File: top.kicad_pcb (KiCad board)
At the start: 2 copper layers, 49.5 x 147.2 mm, 61 parts, among them J1 Conn_01x04, J10 105162-0001, J2 USB_B_Micro, J3 Conn_01x02, J4 Conn_01x02, J5 Conn_01x02, J6 Conn_01x04, J7 Conn_01x02, J8 Conn_01x02, J9 Conn_01x02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

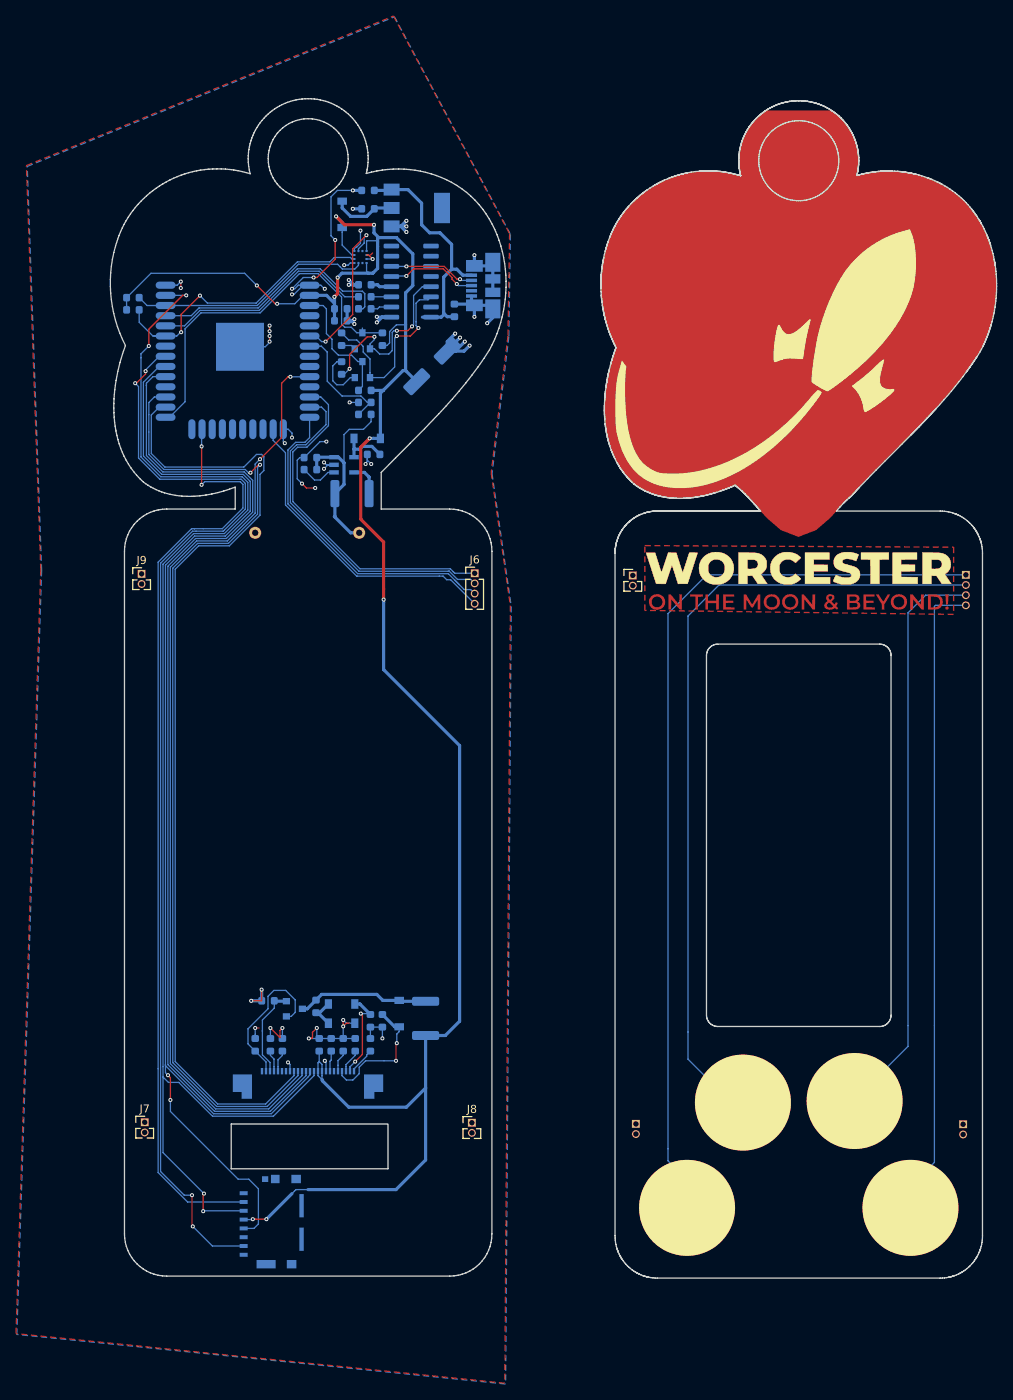
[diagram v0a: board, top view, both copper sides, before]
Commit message: split boards into top and bottom
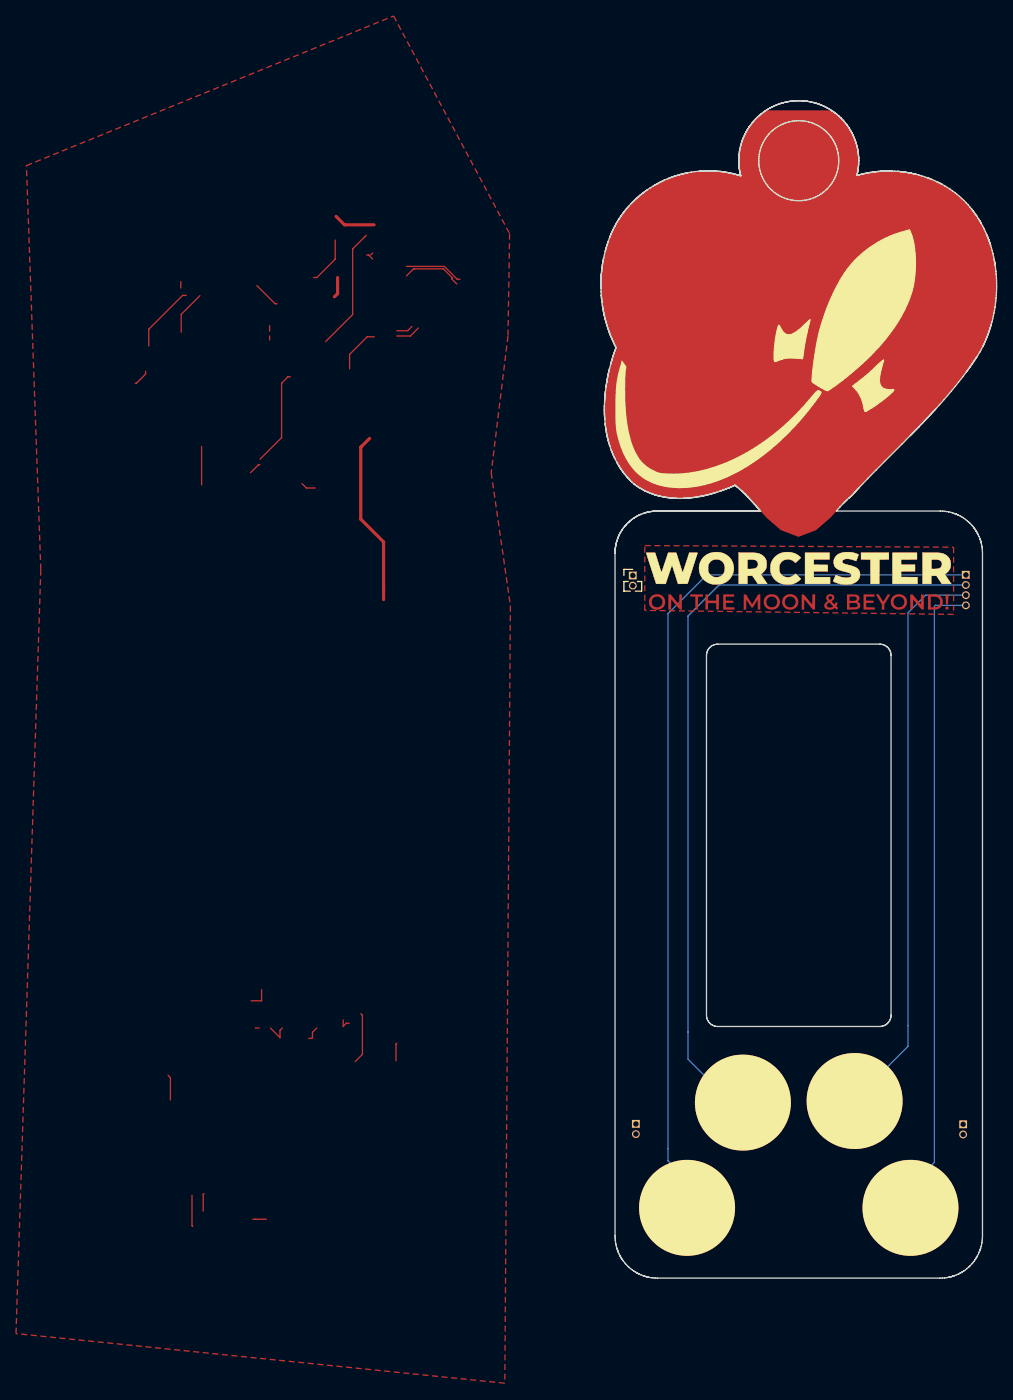
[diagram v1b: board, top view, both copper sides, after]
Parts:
- removed BT1: Battery_Cell, 12BH321P-GR:12BH321P-GR
- removed C1, C17, C2, C3: 10uF, Capacitor_SMD:C_0603_1608Metric
- removed C10, C11, C12, C13, C16, C18, C20, C4, C6, C7, C8, C9: 1uF, Capacitor_SMD:C_0603_1608Metric
- removed C14: 2.2uF, Capacitor_SMD:C_0603_1608Metric
- removed C19: 220uF, Capacitor_SMD:CP_Elec_6.3x5.7
- removed C5: 10uf, Capacitor_SMD:C_0603_1608Metric
- removed D1, D2, D3, D4, D5: D_Schottky, Diode_SMD:D_SOD-123
- removed J10: 105162-0001, 105162-0001:105162-0001
- removed J2: USB_B_Micro, Connector_USB:USB_Micro-B_Molex_47346-0001
- removed J6: Conn_01x04, Connector_PinHeader_1.27mm:PinHeader_1x04_P1.27mm_Vertical
- removed J7, J8, J9: Conn_01x02, Connector_PinHeader_1.27mm:PinHeader_1x02_P1.27mm_Vertical
- removed L1: L, Inductor_SMD:L_1812_4532Metric
- removed L2: 68uH, Inductor_SMD:L_1812_4532Metric
- removed Q1, Q3: PN2222A, Package_TO_SOT_SMD:SOT-23
- removed Q2: Q_NMOS_GSD, Package_TO_SOT_SMD:SOT-23
- removed R1: 10KR, Capacitor_SMD:C_0603_1608Metric
- removed R10, R3, R5, R6: 10K, Capacitor_SMD:C_0603_1608Metric
- removed R11, R8: 1k, Capacitor_SMD:C_0603_1608Metric
- removed R12, R13: 2.2k, Capacitor_SMD:C_0603_1608Metric
- removed R2: DNP, Capacitor_SMD:C_0603_1608Metric
- removed R4: 2.2R, Capacitor_SMD:C_0603_1608Metric
- removed R7, R9: 100k, Capacitor_SMD:C_0603_1608Metric
- removed U1: ESP32-WROOM, ESP32-footprints-Lib:ESP32-WROOM
- removed U2: XC9141, SOT95P280X130-5N:SOT95P280X130-5N
- removed U3: KX122-1037, LGA16R50P4X4_200X200X100:LGA16R50P4X4_200X200X100
- removed U4: AP1117-33, Package_TO_SOT_SMD:SOT-223-3_TabPin2
- removed U5: CH340G, Package_SO:SOIC-16_3.9x9.9mm_P1.27mm
- removed X1: 52435-2471, 52435-2471:MOLEX_52435-2471
- removed the svg2mod at (140.0, 100.0)
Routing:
- net +3V3: track 249.6 -> 34.7 mm, vias 10 -> 0
- net EINK_MOSI: track 168.6 -> 10.8 mm, vias 4 -> 0
- net EINK_SCLK: track 157.8 -> 3.22 mm, vias 2 -> 0
- net MISO: track 138.8 -> 6.07 mm, vias 4 -> 0
- net EINK_CS: track 128.2 -> 0.00 mm
- net EINK_RESET: track 125.8 -> 1.60 mm, vias 2 -> 0
- net EINK_BUSY: track 124.1 -> 0.00 mm
- net GND: track 141.9 -> 21.1 mm, vias 54 -> 0
- net MMC_CS: track 117.3 -> 4.80 mm, vias 2 -> 0
- net EINK_DC: track 118.0 -> 12.0 mm, vias 2 -> 0
- net IO0: track 45.5 -> 0.00 mm
- net T7: track 152.4 -> 108.5 mm
- net T6: track 138.7 -> 95.1 mm
- net T5: track 108.0 -> 66.6 mm
- net T4: track 113.5 -> 74.6 mm
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- removed copper zone on B.Cu, net GND
